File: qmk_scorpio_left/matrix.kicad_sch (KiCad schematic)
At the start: 52 parts

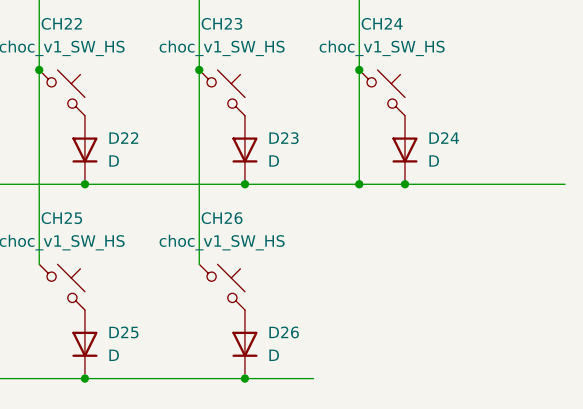
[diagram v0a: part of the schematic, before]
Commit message: placed all components on board
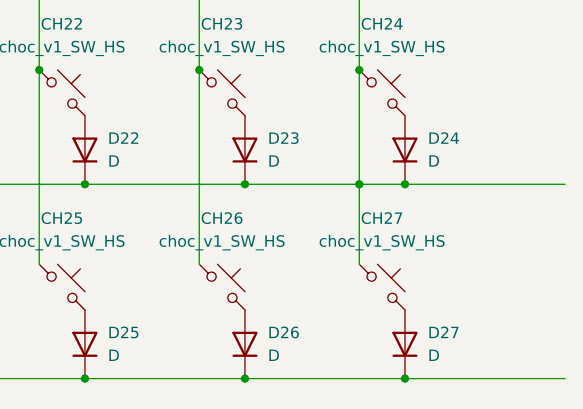
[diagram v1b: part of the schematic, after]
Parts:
- added CH27: choc_v1_SW_HS, PCM_marbastlib-choc:SW_choc_v1_HS_CPG135001S30_1u, symbol PCM_marbastlib-choc:choc_v1_SW_HS_CPG135001S30
- added D27: D, Diode_SMD:D_SOD-123, symbol Device:D
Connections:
- net col0: now also CH27.1
- net row4: now also D27.1 (K)
- new net: CH27.2, D27.2 (A)
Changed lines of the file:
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@@
 	)
 	(junction
+		(at 238.76 171.45)
+		(diameter 0)
+		(color 0 0 0 0)
+	)
+	(junction
 		(at 198.12 69.85)
 		(diameter 0)
@@
 	(wire
 		(pts
-			(xy 220.98 171.45) (xy 228.6 171.45)
+			(xy 220.98 171.45) (xy 238.76 171.45)
 		)
 		(stroke
@@
 	(wire
 		(pts
+			(xy 233.68 149.86) (xy 233.68 158.75)
+		)
+		(stroke
+			(width 0)
+			(type default)
+		)
+	)
+	(wire
+		(pts
 			(xy 238.76 105.41) (xy 256.54 105.41)
 		)
@@
 		)
 	)
+	(wire
+		(pts
+			(xy 238.76 171.45) (xy 256.54 171.45)
+		)
+		(stroke
+			(width 0)
+			(type default)
+		)
+	)
 	(global_label "col2"
 		(shape input)
@@
 	)
 	(symbol
+		(lib_id "Device:D")
+		(at 238.76 167.64 90)
+		(unit 1)
+		(exclude_from_sim no)
+		(in_bom yes)
+		(on_board yes)
+		(dnp no)
+		(fields_autoplaced yes)
+		(property "Reference" "D27"
+			(at 241.3 166.3699 90)
+			(effects
+				(font
+					(size 1.27 1.27)
+				)
+				(justify right)
+			)
+		)
+		(property "Value" "D"
+			(at 241.3 168.9099 90)
+			(effects
+				(font
+					(size 1.27 1.27)
+				)
+				(justify right)
+			)
+		)
+		(property "Footprint" "Diode_SMD:D_SOD-123"
+			(at 238.76 167.64 0)
+			(effects
+				(font
+					(size 1.27 1.27)
+				)
+				(hide yes)
+			)
+		)
+		(property "Datasheet" "~"
+			(at 238.76 167.64 0)
+			(effects
+				(font
+					(size 1.27 1.27)
+				)
+				(hide yes)
+			)
+		)
+		(property "Description" "Diode"
+			(at 238.76 167.64 0)
+			(effects
+				(font
+					(size 1.27 1.27)
+				)
+				(hide yes)
+			)
+		)
+		(property "Sim.Device" "D"
+			(at 238.76 167.64 0)
+			(effects
+				(font
+					(size 1.27 1.27)
+				)
+				(hide yes)
+			)
+		)
+		(property "Sim.Pins" "1=K 2=A"
+			(at 238.76 167.64 0)
+			(effects
+				(font
+					(size 1.27 1.27)
+				)
+				(hide yes)
+			)
+		)
+		(pin "1"
+		)
+		(pin "2"
+		)
+		(instances
+			(project "qmk_scorpio_left"
+				(path "/cb32b2da-a60d-4ed4-a57b-2c397f553171/d515a0f5-02b9-43be-9c9a-ca0ce99df960"
+					(reference "D27")
+					(unit 1)
+				)
+			)
+		)
+	)
+	(symbol
 		(lib_id "PCM_marbastlib-choc:choc_v1_SW_HS_CPG135001S30")
 		(at 236.22 139.7 0)
@@
 					(unit 1)
 				)
+			)
+		)
+	)
+	(symbol
+		(lib_id "PCM_marbastlib-choc:choc_v1_SW_HS_CPG135001S30")
+		(at 236.22 161.29 0)
+		(unit 1)
+		(exclude_from_sim no)
+		(in_bom yes)
+		(on_board yes)
+		(dnp no)
+		(fields_autoplaced yes)
+		(property "Reference" "CH27"
+			(at 236.22 153.67 0)
+			(effects
+				(font
+					(size 1.27 1.27)
+				)
+			)
+		)
+		(property "Value" "choc_v1_SW_HS"
+			(at 236.22 156.21 0)
+			(effects
+				(font
+					(size 1.27 1.27)
+				)
+			)
+		)
+		(property "Footprint" "PCM_marbastlib-choc:SW_choc_v1_HS_CPG135001S30_1u"
+			(at 236.22 161.29 0)
+			(effects
+				(font
+					(size 1.27 1.27)
+				)
+				(hide yes)
+			)
+		)
+		(property "Datasheet" "~"
+			(at 236.22 161.29 0)
+			(effects
+				(font
+					(size 1.27 1.27)
+				)
+				(hide yes)
+			)
+		)
+		(property "Description" "Push button switch, normally open, two pins, 45° tilted"
+			(at 236.22 161.29 0)
+			(effects
+				(font
+					(size 1.27 1.27)
+				)
+				(hide yes)
+			)
+		)
+		(pin "2"
+		)
+		(pin "1"
+		)
+		(instances
+			(project "qmk_scorpio_left"
+				(path "/cb32b2da-a60d-4ed4-a57b-2c397f553171/d515a0f5-02b9-43be-9c9a-ca0ce99df960"
+					(reference "CH27")
+					(unit 1)
+				)

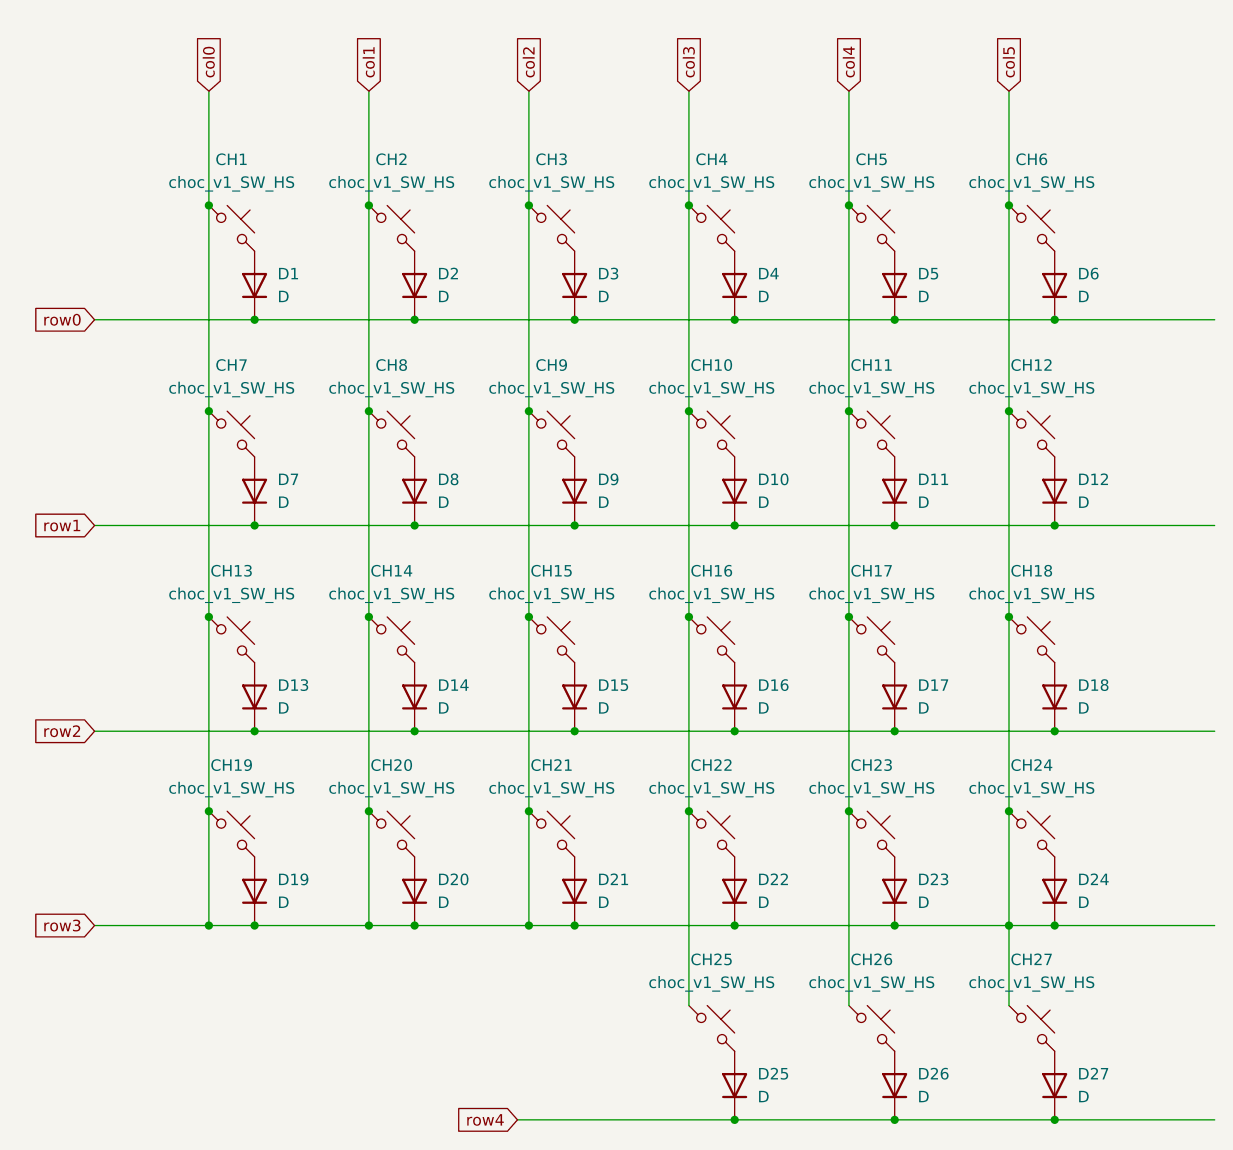
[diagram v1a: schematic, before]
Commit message: fixed col/row connections in matrix schematics
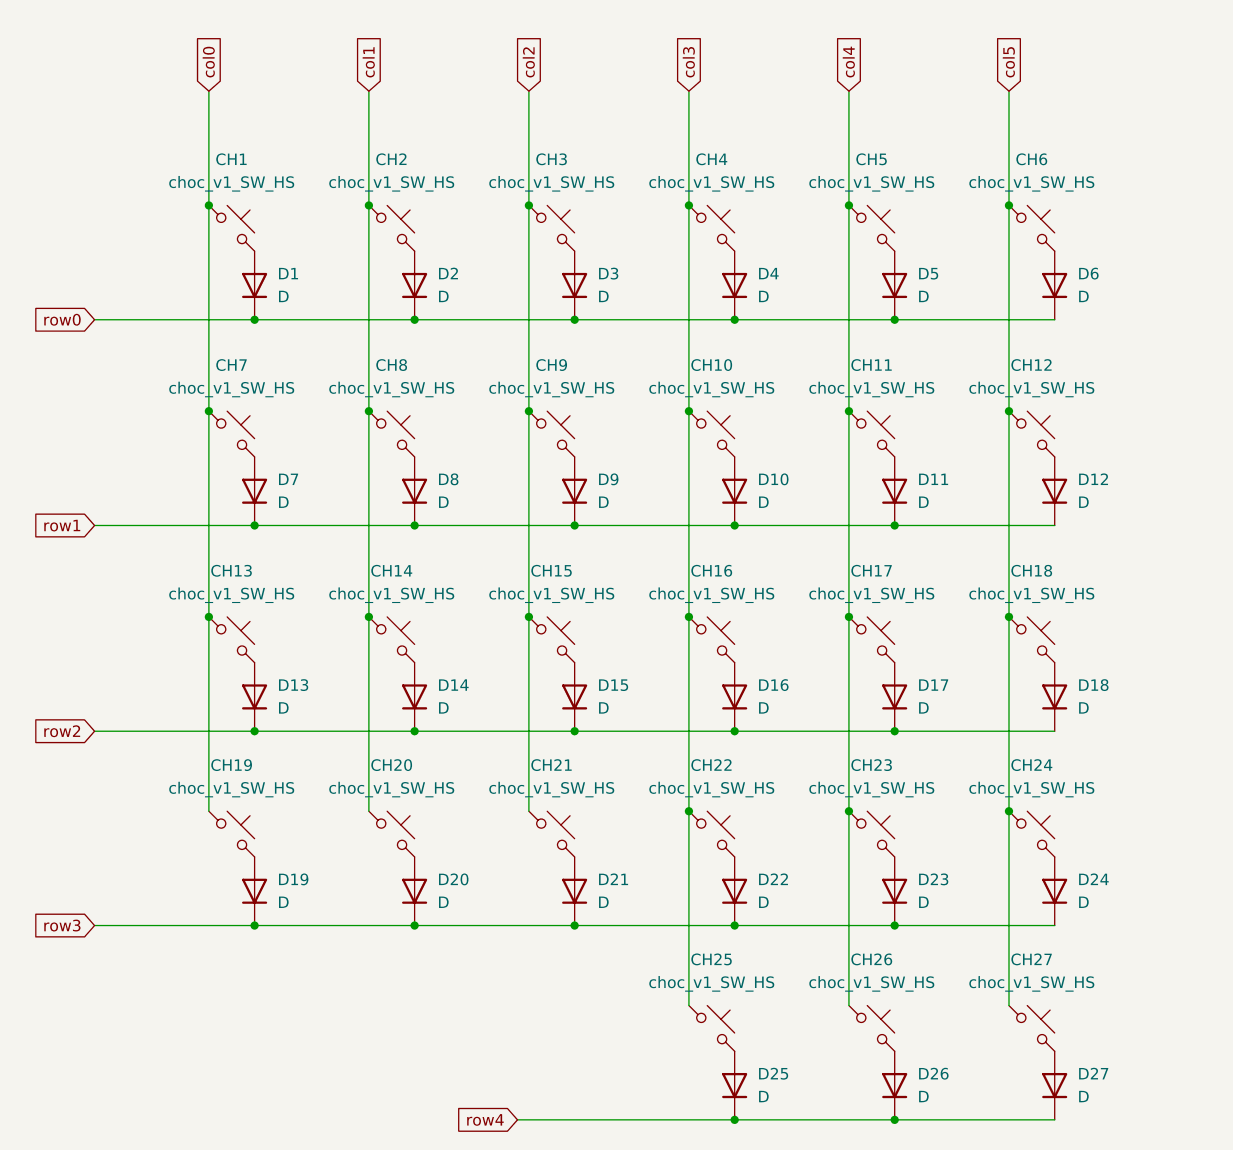
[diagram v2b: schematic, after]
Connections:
- net col0: no longer CH12.1, CH14.1, CH15.1, CH18.1, CH2.1, CH20.1, CH21.1, CH24.1, CH27.1, CH3.1, CH6.1, CH8.1, CH9.1, D19.1 (K), D20.1 (K), D21.1 (K), D22.1 (K), D23.1 (K), D24.1 (K)
- new net col1: CH14.1, CH2.1, CH20.1, CH8.1
- new net col2: CH15.1, CH21.1, CH3.1, CH9.1
- new net col5: CH12.1, CH18.1, CH24.1, CH27.1, CH6.1
- new net row3: D19.1 (K), D20.1 (K), D21.1 (K), D22.1 (K), D23.1 (K), D24.1 (K)
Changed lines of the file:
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@@
-	)
-	(junction
-		(at 238.76 171.45)
-		(diameter 0)
-		(color 0 0 0 0)
 	)
 	(junction
@@
 	)
 	(junction
-		(at 238.76 128.27)
-		(diameter 0)
-		(color 0 0 0 0)
-	)
-	(junction
 		(at 162.56 69.85)
 		(diameter 0)
@@
 	)
 	(junction
-		(at 180.34 149.86)
-		(diameter 0)
-		(color 0 0 0 0)
-	)
-	(junction
 		(at 144.78 115.57)
 		(diameter 0)
@@
 	)
 	(junction
-		(at 180.34 137.16)
-		(diameter 0)
-		(color 0 0 0 0)
-	)
-	(junction
 		(at 149.86 82.55)
 		(diameter 0)
@@
 	)
 	(junction
-		(at 162.56 137.16)
-		(diameter 0)
-		(color 0 0 0 0)
-	)
-	(junction
 		(at 167.64 105.41)
 		(diameter 0)
@@
 	)
 	(junction
-		(at 144.78 137.16)
-		(diameter 0)
-		(color 0 0 0 0)
-	)
-	(junction
 		(at 220.98 128.27)
 		(diameter 0)
@@
 	)
 	(junction
-		(at 233.68 149.86)
-		(diameter 0)
-		(color 0 0 0 0)
-	)
-	(junction
 		(at 162.56 115.57)
 		(diameter 0)
@@
 	)
 	(junction
-		(at 238.76 149.86)
-		(diameter 0)
-		(color 0 0 0 0)
-	)
-	(junction
 		(at 185.42 105.41)
 		(diameter 0)
@@
 	)
 	(junction
-		(at 238.76 82.55)
-		(diameter 0)
-		(color 0 0 0 0)
-	)
-	(junction
 		(at 185.42 82.55)
 		(diameter 0)
@@
 	)
 	(junction
-		(at 162.56 149.86)
-		(diameter 0)
-		(color 0 0 0 0)
-	)
-	(junction
 		(at 203.2 128.27)
 		(diameter 0)
@@
 	)
 	(junction
-		(at 238.76 105.41)
-		(diameter 0)
-		(color 0 0 0 0)
-	)
-	(junction
 		(at 198.12 115.57)
 		(diameter 0)
@@
 	)
 	(junction
-		(at 144.78 149.86)
-		(diameter 0)
-		(color 0 0 0 0)
-	)
-	(junction
 		(at 149.86 149.86)
 		(diameter 0)
@@
 	(wire
 		(pts
-			(xy 167.64 149.86) (xy 180.34 149.86)
+			(xy 167.64 149.86) (xy 185.42 149.86)
 		)
 		(stroke
@@
 	(wire
 		(pts
-			(xy 149.86 149.86) (xy 162.56 149.86)
+			(xy 149.86 149.86) (xy 167.64 149.86)
 		)
 		(stroke
@@
 	(wire
 		(pts
-			(xy 220.98 149.86) (xy 233.68 149.86)
-		)
-		(stroke
-			(width 0)
-			(type default)
-		)
-	)
-	(wire
-		(pts
-			(xy 238.76 149.86) (xy 256.54 149.86)
+			(xy 220.98 149.86) (xy 238.76 149.86)
 		)
 		(stroke
@@
 	(wire
 		(pts
-			(xy 144.78 137.16) (xy 144.78 149.86)
-		)
-		(stroke
-			(width 0)
-			(type default)
-		)
-	)
-	(wire
-		(pts
 			(xy 220.98 171.45) (xy 238.76 171.45)
 		)
@@
 	(wire
 		(pts
-			(xy 238.76 82.55) (xy 256.54 82.55)
-		)
-		(stroke
-			(width 0)
-			(type default)
-		)
-	)
-	(wire
-		(pts
 			(xy 220.98 105.41) (xy 238.76 105.41)
 		)
@@
 	(wire
 		(pts
-			(xy 162.56 149.86) (xy 167.64 149.86)
-		)
-		(stroke
-			(width 0)
-			(type default)
-		)
-	)
-	(wire
-		(pts
-			(xy 233.68 149.86) (xy 238.76 149.86)
-		)
-		(stroke
-			(width 0)
-			(type default)
-		)
-	)
-	(wire
-		(pts
 			(xy 215.9 57.15) (xy 215.9 69.85)
 		)
@@
 	(wire
 		(pts
-			(xy 233.68 149.86) (xy 233.68 158.75)
-		)
-		(stroke
-			(width 0)
-			(type default)
-		)
-	)
-	(wire
-		(pts
-			(xy 238.76 105.41) (xy 256.54 105.41)
+			(xy 233.68 137.16) (xy 233.68 158.75)
 		)
 		(stroke
@@
 	(wire
 		(pts
-			(xy 162.56 137.16) (xy 162.56 149.86)
-		)
-		(stroke
-			(width 0)
-			(type default)
-		)
-	)
-	(wire
-		(pts
 			(xy 203.2 105.41) (xy 220.98 105.41)
 		)
@@
 	(wire
 		(pts
-			(xy 180.34 137.16) (xy 180.34 149.86)
-		)
-		(stroke
-			(width 0)
-			(type default)
-		)
-	)
-	(wire
-		(pts
 			(xy 149.86 82.55) (xy 167.64 82.55)
 		)
@@
 	(wire
 		(pts
-			(xy 238.76 128.27) (xy 256.54 128.27)
-		)
-		(stroke
-			(width 0)
-			(type default)
-		)
-	)
-	(wire
-		(pts
 			(xy 215.9 69.85) (xy 215.9 92.71)
 		)
@@
 	(wire
 		(pts
-			(xy 180.34 149.86) (xy 185.42 149.86)
-		)
-		(stroke
-			(width 0)
-			(type default)
-		)
-	)
-	(wire
-		(pts
-			(xy 144.78 149.86) (xy 149.86 149.86)
-		)
-		(stroke
-			(width 0)
-			(type default)
-		)
-	)
-	(wire
-		(pts
-			(xy 132.08 149.86) (xy 144.78 149.86)
+			(xy 132.08 149.86) (xy 149.86 149.86)
 		)
 		(stroke
@@
 	(wire
 		(pts
-			(xy 233.68 137.16) (xy 233.68 149.86)
-		)
-		(stroke
-			(width 0)
-			(type default)
-		)
-	)
-	(wire
-		(pts
 			(xy 185.42 128.27) (xy 203.2 128.27)
 		)
@@
 		)
 		(stroke
-			(width 0)
-			(type default)
-		)
-	)
-	(wire
-		(pts
-			(xy 238.76 171.45) (xy 256.54 171.45)
-		)
-		(stroke
